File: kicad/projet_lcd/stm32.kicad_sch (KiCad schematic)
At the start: 36 parts, among them U1 STM32H563ZIT6, Y1 25MHZ, Y2 32.768KHZ

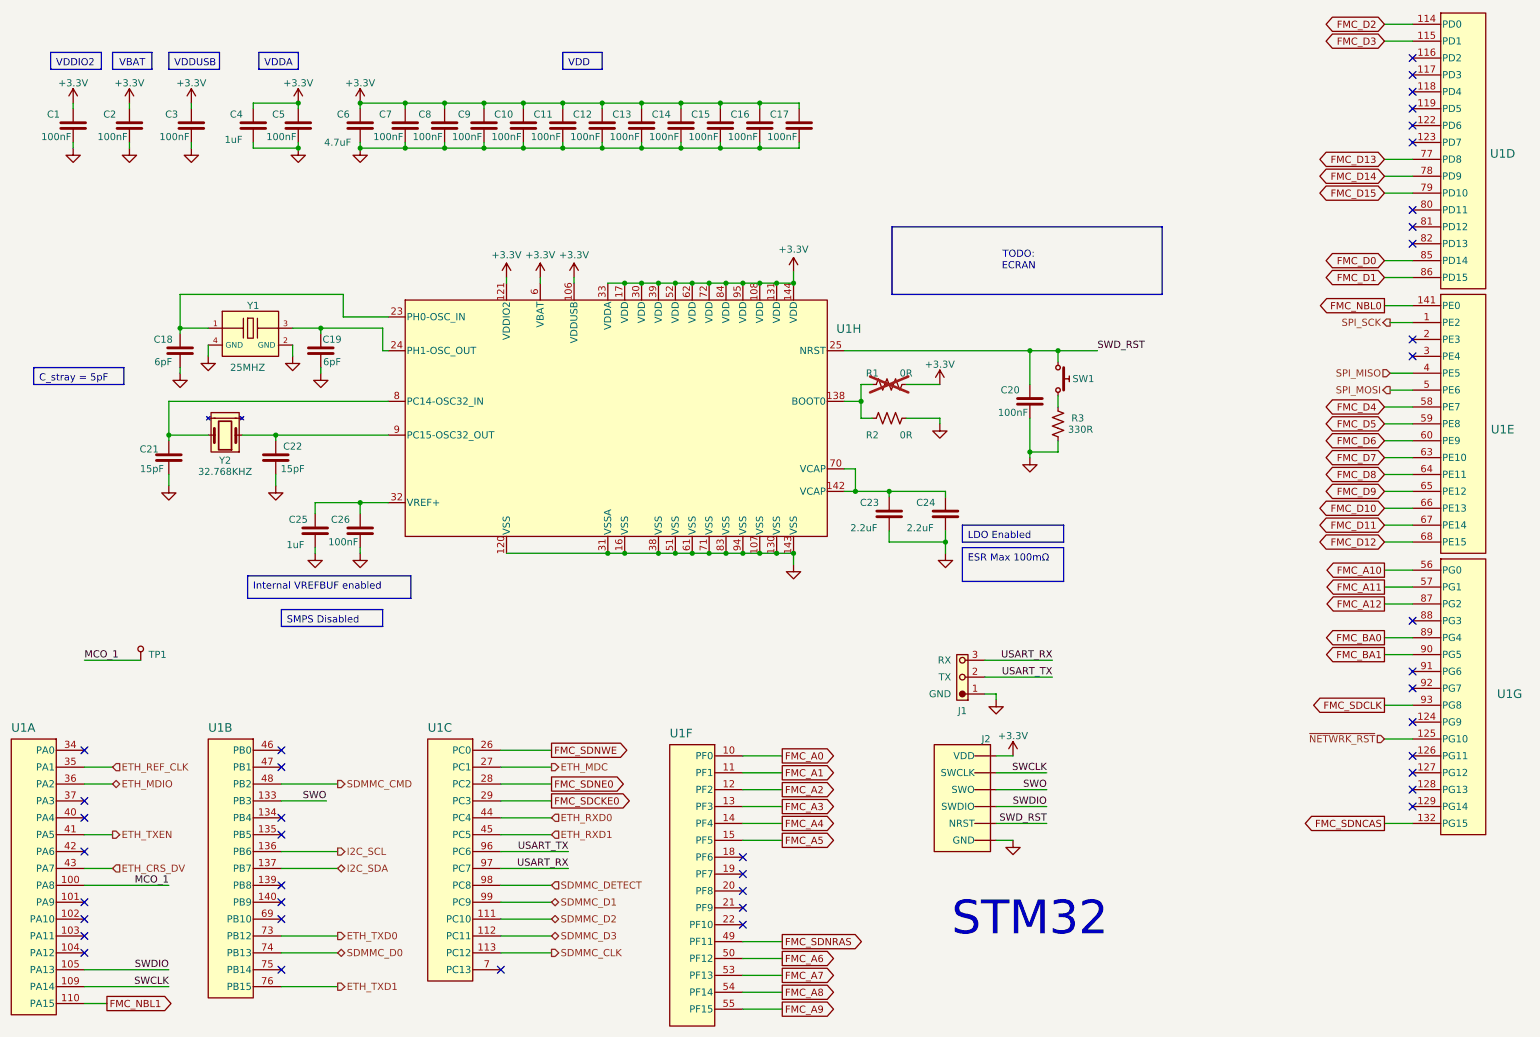
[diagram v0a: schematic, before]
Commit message: cleaning up ERC alerts
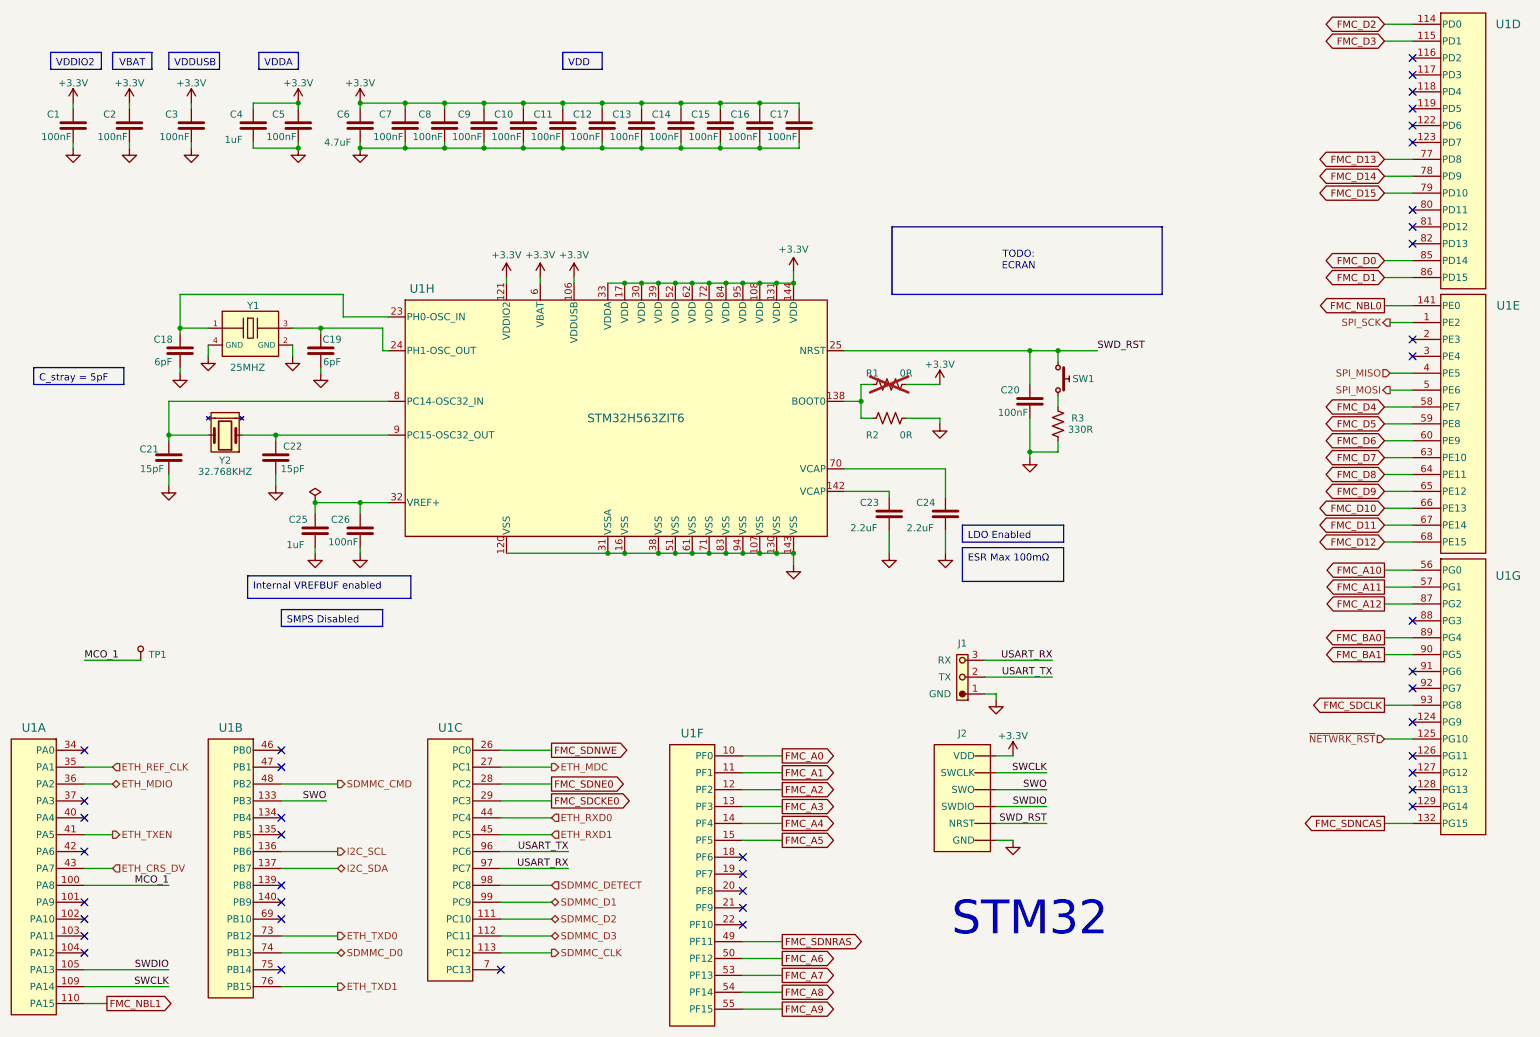
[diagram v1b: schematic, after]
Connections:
- net at C23.2, U1.142 (VCAP): no longer C24.2, U1.70 (VCAP)
- new net: C24.2, U1.70 (VCAP)
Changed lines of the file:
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@@
 	)
 	(junction
-		(at 77 30)
+		(at 69 101)
 		(diameter 0)
 		(color 0 0 0 0)
 	)
 	(junction
-		(at 85 30)
+		(at 77 30)
 		(diameter 0)
 		(color 0 0 0 0)
 	)
 	(junction
-		(at 124 110)
+		(at 85 30)
 		(diameter 0)
 		(color 0 0 0 0)
 	)
 	(junction
-		(at 196 74)
+		(at 124 110)
 		(diameter 0)
 		(color 0 0 0 0)
 	)
 	(junction
-		(at 165 99)
+		(at 196 74)
 		(diameter 0)
 		(color 0 0 0 0)
@@
 	)
 	(junction
-		(at 181 108)
-		(diameter 0)
-		(color 0 0 0 0)
-	)
-	(junction
 		(at 62 89)
 		(diameter 0)
@@
 	)
 	(junction
-		(at 171 99)
-		(diameter 0)
-		(color 0 0 0 0)
-	)
-	(junction
 		(at 92 30)
 		(diameter 0)
@@
 	(wire
 		(pts
-			(xy 171 99) (xy 181 99)
-		)
-		(stroke
-			(width 0)
-			(type default)
-		)
-	)
-	(wire
-		(pts
 			(xy 133 110) (xy 136 110)
 		)
@@
 	(wire
 		(pts
-			(xy 181 108) (xy 181 110)
-		)
-		(stroke
-			(width 0)
-			(type default)
-		)
-	)
-	(wire
-		(pts
 			(xy 134 38) (xy 134 37)
 		)
@@
 	(wire
 		(pts
-			(xy 165 99) (xy 171 99)
+			(xy 163 99) (xy 171 99)
 		)
 		(stroke
@@
 	(wire
 		(pts
-			(xy 165 95) (xy 163 95)
-		)
-		(stroke
-			(width 0)
-			(type default)
-		)
-	)
-	(wire
-		(pts
 			(xy 259 99) (xy 264 99)
 		)
@@
 	(wire
 		(pts
-			(xy 165 95) (xy 165 99)
-		)
-		(stroke
-			(width 0)
-			(type default)
-		)
-	)
-	(wire
-		(pts
 			(xy 259 116) (xy 264 116)
 		)
@@
 	(wire
 		(pts
-			(xy 181 99) (xy 181 100)
+			(xy 181 95) (xy 181 100)
 		)
 		(stroke
@@
 	(wire
 		(pts
-			(xy 163 99) (xy 165 99)
-		)
-		(stroke
-			(width 0)
-			(type default)
-		)
-	)
-	(wire
-		(pts
 			(xy 99 30) (xy 99 31)
 		)
@@
 	(wire
 		(pts
-			(xy 181 108) (xy 181 106)
+			(xy 181 106) (xy 181 110)
 		)
 		(stroke
@@
 	(wire
 		(pts
-			(xy 171 108) (xy 181 108)
-		)
-		(stroke
-			(width 0)
-			(type default)
-		)
-	)
-	(wire
-		(pts
 			(xy 120 38) (xy 127 38)
 		)
@@
 	(wire
 		(pts
-			(xy 171 106) (xy 171 108)
+			(xy 171 106) (xy 171 110)
 		)
 		(stroke
@@
 	(wire
 		(pts
+			(xy 163 95) (xy 181 95)
+		)
+		(stroke
+			(width 0)
+			(type default)
+		)
+	)
+	(wire
+		(pts
 			(xy 63 166) (xy 73 166)
 		)
@@
 	)
 	(symbol
+		(lib_name "STM32H563ZIT6_4")
 		(lib_id "MicroControllers:STM32H563ZIT6")
 		(at 82 65 0)
@@
 		(on_board yes)
 		(dnp no)
-		(fields_autoplaced yes)
 		(property "Reference" "U1"
-			(at 163.83 70.1198 0)
+			(at 88 63 0)
 			(effects
 				(font
@@
 		)
 		(property "Value" "STM32H563ZIT6"
-			(at 90 49 0)
+			(at 126 86 0)
 			(effects
 				(font
 					(size 1.524 1.524)
 				)
-				(hide yes)
 			)
 		)
@@
 	)
 	(symbol
+		(lib_name "STM32H563ZIT6_6")
 		(lib_id "MicroControllers:STM32H563ZIT6")
 		(at 28 145 0)
@@
 		(dnp no)
 		(property "Reference" "U1"
-			(at 15 141 0)
+			(at 19 141 0)
 			(effects
 				(font
 					(size 1.524 1.524)
 				)
-				(justify right)
 			)
 		)
@@
 		(dnp no)
 		(property "Reference" "U1"
-			(at 279 135 0)
+			(at 281 114 0)
 			(effects
 				(font
 					(size 1.524 1.524)
 				)
-				(justify left)
 			)
 		)
@@
 		(dnp no)
 		(property "Reference" "U1"
-			(at 280 39 0)
+			(at 281 16 0)
 			(effects
 				(font
@@
 		(dnp no)
 		(property "Reference" "U1"
-			(at 89 141 0)
+			(at 93 141 0)
 			(effects
 				(font
 					(size 1.524 1.524)
 				)
-				(justify right)
 			)
 		)
@@
 		(on_board yes)
 		(dnp no)
-		(fields_autoplaced yes)
 		(property "Reference" "J2"
-			(at 189 143 0)
+			(at 184 142 0)
 			(do_not_autoplace yes)
 			(effects
@@
 					(size 1.25 1.25)
 				)
-				(justify left)
 			)
 		)
@@
 		(dnp no)
 		(property "Reference" "J1"
-			(at 184 138 0)
+			(at 184 126 0)
 			(do_not_autoplace yes)
 			(effects
@@
 	)
 	(symbol
+		(lib_id "Power:GND")
+		(at 171 110 0)
+		(unit 1)
+		(exclude_from_sim no)
+		(in_bom yes)
+		(on_board yes)
+		(dnp no)
+		(fields_autoplaced yes)
+		(property "Reference" "#PWR097"
+			(at 171 116.35 0)
+			(effects
+				(font
+					(size 1.25 1.25)
+				)
+				(hide yes)
+			)
+		)
+		(property "Value" "GND"
+			(at 171 113.81 0)
+			(effects
+				(font
+					(size 1.25 1.25)
+				)
+				(hide yes)
+			)
+		)
+		(property "Footprint" ""
+			(at 171 110 0)
+			(effects
+				(font
+					(size 1.25 1.25)
+				)
+				(hide yes)
+			)
+		)
+		(property "Datasheet" ""
+			(at 171 110 0)
+			(effects
+				(font
+					(size 1.25 1.25)
+				)
+				(hide yes)
+			)
+		)
+		(property "Description" "Power symbol creates a global label with name \"GND\""
+			(at 173.54 120.668 0)
+			(effects
+				(font
+					(size 1.25 1.25)
+				)
+				(hide yes)
+			)
+		)
+		(pin "1"
+		)
+		(instances
+			(project "projet_lcd"
+				(path "/b3ce22de-813e-4a84-80c2-bec39c904000/9ea47d51-491e-4a8f-867a-699065ac1e83"
+					(reference "#PWR097")
+					(unit 1)
+				)
+			)
+		)
+	)
+	(symbol
 		(lib_id "Power:+3.3V")
 		(at 26 30 0)
@@
 		(dnp no)
 		(property "Reference" "U1"
-			(at 280 88 0)
+			(at 281 66 0)
 			(effects
 				(font
@@
 	)
 	(symbol
+		(lib_id "Power:PWR_FLAG")
+		(at 69 101 0)
+		(unit 1)
+		(exclude_from_sim no)
+		(in_bom yes)
+		(on_board yes)
+		(dnp no)
+		(fields_autoplaced yes)
+		(property "Reference" "#FLG07"
+			(at 69.5 114.5 0)
+			(effects
+				(font
+					(size 1.25 1.25)
+				)
+				(hide yes)
+			)
+		)
+		(property "Value" "PWR_FLAG"
+			(at 69 117 0)
+			(effects
+				(font
+					(size 1.25 1.25)
+				)
+				(hide yes)
+			)
+		)
+		(property "Footprint" ""
+			(at 69 101 0)
+			(effects
+				(font
+					(size 1.25 1.25)
+				)
+				(hide yes)
+			)
+		)
+		(property "Datasheet" ""
+			(at 69 101 0)
+			(effects
+				(font
+					(size 1.25 1.25)
+				)
+				(hide yes)
+			)
+		)
+		(property "Description" "Kicad strange way of managing power input/output pins"
+			(at 69 112 0)
+			(effects
+				(font
+					(size 1.25 1.25)
+				)
+				(hide yes)
+			)
+		)
+		(pin "1"
+		)
+		(instances
+			(project ""
+				(path "/b3ce22de-813e-4a84-80c2-bec39c904000/9ea47d51-491e-4a8f-867a-699065ac1e83"
+					(reference "#FLG07")
+					(unit 1)
+				)
+			)
+		)
+	)
+	(symbol
+		(lib_name "STM32H563ZIT6_5")
 		(lib_id "MicroControllers:STM32H563ZIT6")
 		(at 63 145 0)
@@
 		(dnp no)
 		(property "Reference" "U1"
-			(at 50 141 0)
+			(at 54 141 0)
 			(effects
 				(font
 					(size 1.524 1.524)
 				)
-				(justify right)
 			)
 		)
@@
 		(dnp no)
 		(property "Reference" "U1"
-			(at 132 142 0)
+			(at 136 142 0)
 			(effects
 				(font
 					(size 1.524 1.524)
 				)
-				(justify right)
 			)
 		)

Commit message: on avance !
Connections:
- net ETH_TXD1: now also U1.127 (PG12); no longer U1.76 (PB15)
- net SPI_MISO: now also U1.75 (PB14); no longer U1.4 (PE5)
- net SPI_MOSI: now also U1.76 (PB15); no longer U1.5 (PE6)
- net SPI_SCK: now also U1.69 (PB10); no longer U1.1 (PE2)
- net USART_RX: now also U1.102 (PA10); no longer U1.97 (PC7)
- net USART_TX: now also U1.101 (PA9); no longer U1.96 (PC6)
- net USB_DM: now reaches U1.103 (PA11)
- net USB_DP: now reaches U1.104 (PA12)
- net DISPLAY_MISO: now reaches U1.42 (PA6)
- net DISPLAY_CLK: now reaches U1.126 (PG11)
- net OUTPUT_9: now reaches U1.129 (PG14)
- net DISPLAY_PWM: now reaches U1.88 (PG3)
- net OUTPUT_7: now reaches U1.91 (PG6)
- net OUTPUT_2: now reaches U1.118 (PD4)
- net DISPLAY_MOSI: now reaches U1.123 (PD7)
- net DISPLAY_RST: now reaches U1.80 (PD11)
- net DISPLAY_RS: now reaches U1.81 (PD12)
- net DISPLAY_CS: now reaches U1.82 (PD13)
- net OUTPUT_3: now reaches U1.2 (PE3)
- net OUTPUT_4: now reaches U1.18 (PF6)
- net OUTPUT_5: now reaches U1.20 (PF8)
- net OUTPUT_6: now reaches U1.21 (PF9)
- net OUTPUT_8: now reaches U1.22 (PF10)
- new net OUTPUT_0: U1.96 (PC6)
- new net OUTPUT_1: U1.97 (PC7)
- no-connect marks 41 -> 22
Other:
- note removed: "TODO: ECRAN"

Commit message: routage en cours
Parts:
- J1: PIN_01 GND -> ## PIN1; PIN_02 TX -> ## PIN2; PIN_03 RX -> ## PIN3
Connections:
- net USB_DM: no longer names the net of U1.103 (PA11)
- net USB_DP: no longer names the net of U1.104 (PA12)
- no-connect marks 22 -> 24
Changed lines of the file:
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@@
 		)
 	)
+	(text_box "USB for later use ..."
+		(exclude_from_sim no)
+		(at 30 176 0)
+		(size 18 5)
+		(margins 0.9525 0.9525 0.9525 0.9525)
+		(stroke
+			(width 0)
+			(type solid)
+		)
+		(fill
+			(type none)
+		)
+		(effects
+			(font
+				(size 1.27 1.27)
+			)
+			(justify left top)
+		)
+	)
 	(text_box "VDDA"
 		(exclude_from_sim no)
@@
 	)
 	(no_connect
+		(at 28 178)
+	)
+	(no_connect
 		(at 28 157)
 	)
@@
 	)
 	(no_connect
+		(at 28 181)
+	)
+	(no_connect
 		(at 63 160)
 	)
@@
 	(wire
 		(pts
-			(xy 28 178) (xy 43 178)
-		)
-		(stroke
-			(width 0)
-			(type default)
-		)
-	)
-	(wire
-		(pts
-			(xy 28 181) (xy 43 181)
-		)
-		(stroke
-			(width 0)
-			(type default)
-		)
-	)
-	(wire
-		(pts
 			(xy 196 74) (xy 201 74)
 		)
@@
 		)
 	)
-	(label "USB_DM"
-		(at 43 178 180)
-		(effects
-			(font
-				(size 1.27 1.27)
-			)
-			(justify right bottom)
-		)
-	)
 	(label "SWDIO"
 		(at 43 184 180)
@@
 		)
 	)
-	(label "USB_DP"
-		(at 43 181 180)
-		(effects
-			(font
-				(size 1.27 1.27)
-			)
-			(justify right bottom)
-		)
-	)
 	(global_label "FMC_SDNRAS"
 		(shape output)
@@
 	)
 	(symbol
-		(lib_name "STM32H563ZIT6_4")
 		(lib_id "MicroControllers:STM32H563ZIT6")
 		(at 82 65 0)
@@
 	)
 	(symbol
-		(lib_name "STM32H563ZIT6_6")
 		(lib_id "MicroControllers:STM32H563ZIT6")
 		(at 28 145 0)
@@
 			)
 		)
-		(property "PIN_01" "GND"
+		(property "PIN_01" "## PIN1"
 			(at 182 135 0)
 			(do_not_autoplace yes)
@@
 			)
 		)
-		(property "PIN_02" "TX"
+		(property "PIN_02" "## PIN2"
 			(at 182 132 0)
 			(do_not_autoplace yes)
@@
 			)
 		)
-		(property "PIN_03" "RX"
+		(property "PIN_03" "## PIN3"
 			(at 182 129 0)
 			(do_not_autoplace yes)
@@
 	)
 	(symbol
-		(lib_name "STM32H563ZIT6_5")
 		(lib_id "MicroControllers:STM32H563ZIT6")
 		(at 63 145 0)

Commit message: schematiks seems okayish
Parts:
- removed SW1: ~, symbol Generics:SW_PushButton
- added SW1: ~, Misc:C284397, symbol Misc:sw_C2844397
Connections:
- net SWD_RST: now also SW1.1, SW1.2
- net at R3.2 (1): now also SW1.3, SW1.4
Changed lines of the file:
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@@
 	)
 	(symbol
+		(lib_id "Misc:sw_C2844397")
+		(at 201 76 270)
+		(unit 1)
+		(exclude_from_sim no)
+		(in_bom yes)
+		(on_board yes)
+		(dnp no)
+		(fields_autoplaced yes)
+		(property "Reference" "SW1"
+			(at 205.01 77.7299 90)
+			(effects
+				(font
+					(size 1.27 1.27)
+				)
+				(justify left)
+			)
+		)
+		(property "Value" "~"
+			(at 205.01 80.2699 90)
+			(effects
+				(font
+					(size 1.27 1.27)
+				)
+				(justify left)
+				(hide yes)
+			)
+		)
+		(property "Footprint" "Misc:C284397"
+			(at 208.5 79.5 0)
+			(effects
+				(font
+					(size 1.27 1.27)
+				)
+				(hide yes)
+			)
+		)
+		(property "Datasheet" ""
+			(at 201 76 0)
+			(effects
+				(font
+					(size 1.27 1.27)
+				)
+				(hide yes)
+			)
+		)
+		(property "Description" "Switch SPST"
+			(at 206 80 0)
+			(effects
+				(font
+					(size 1.27 1.27)
+				)
+				(hide yes)
+			)
+		)
+		(property "LCSC Part #" "C2844397"
+			(at 210.5 79.5 0)
+			(effects
+				(font
+					(size 1.27 1.27)
+				)
+				(hide yes)
+			)
+		)
+		(pin "3"
+		)
+		(pin "4"
+		)
+		(pin "2"
+		)
+		(pin "1"
+		)
+		(instances
+			(project ""
+				(path "/b3ce22de-813e-4a84-80c2-bec39c904000/9ea47d51-491e-4a8f-867a-699065ac1e83"
+					(reference "SW1")
+					(unit 1)
+				)
+			)
+		)
+	)
+	(symbol
 		(lib_id "Generics:C")
 		(at 47 37 90)
@@
 					(unit 1)
 				)
-			)
-		)
-	)
-	(symbol
-		(lib_id "Generics:SW_PushButton")
-		(at 201 76 270)
-		(unit 1)
-		(exclude_from_sim no)
-		(in_bom yes)
-		(on_board yes)
-		(dnp no)
-		(property "Reference" "SW1"
-			(at 205.5 79 90)
-			(do_not_autoplace yes)
-			(effects
-				(font
-					(size 1.25 1.25)
-				)
-			)
-		)
-		(property "Value" "~"
-			(at 190 80 0)
-			(effects
-				(font
-					(size 1.25 1.25)
-				)
-				(hide yes)
-			)
-		)
-		(property "Footprint" ""
-			(at 206.08 81 0)
-			(effects
-				(font
-					(size 1.25 1.25)
-				)
-				(hide yes)
-			)
-		)
-		(property "Datasheet" ""
-			(at 188 80 0)
-			(effects
-				(font
-					(size 1.25 1.25)
-				)
-				(hide yes)
-			)
-		)
-		(property "Description" "Push button switch, generic, two pins"
-			(at 197.1 79 0)
-			(effects
-				(font
-					(size 1.25 1.25)
-				)
-				(hide yes)
-			)
-		)
-		(property "Part#" ""
-			(at 201 76 0)
-			(effects
-				(font
-					(size 1.25 1.25)
-				)
-				(hide yes)
-			)
-		)
-		(property "Comments" ""
-			(at 201 76 0)
-			(effects
-				(font
-					(size 1.25 1.25)
-				)
-				(hide yes)
-			)
-		)
-		(pin "1"
-		)
-		(pin "2"
-		)
-		(instances
-			(project ""
-				(path "/b3ce22de-813e-4a84-80c2-bec39c904000/9ea47d51-491e-4a8f-867a-699065ac1e83"
-					(reference "SW1")
-					(unit 1)
-				)

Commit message: DRC / ERC ok
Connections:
- net LED_1: now reaches U1.1 (PE2)
- net LED_2: now reaches U1.3 (PE4)
- net LED_3: now reaches U1.4 (PE5)
- net LED_4: now reaches U1.140 (PB9)
- no-connect marks 24 -> 20
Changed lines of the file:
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@@
 		)
 	)
-	(text_box "Ajouter connecteur USB"
-		(exclude_from_sim no)
-		(at 113 122 0)
-		(size 27 5)
-		(margins 0.9525 0.9525 0.9525 0.9525)
-		(stroke
-			(width 0)
-			(type solid)
-		)
-		(fill
-			(type none)
-		)
-		(effects
-			(font
-				(size 1.27 1.27)
-				(color 255 3 64 1)
-			)
-			(justify left top)
-		)
-	)
 	(text_box "VDD\n"
 		(exclude_from_sim no)
@@
 	)
 	(no_connect
-		(at 63 172)
-	)
-	(no_connect
 		(at 264 140)
 	)
@@
 	)
 	(no_connect
-		(at 264 69)
-	)
-	(no_connect
 		(at 264 25)
 	)
@@
 	)
 	(no_connect
-		(at 264 75)
-	)
-	(no_connect
-		(at 264 78)
-	)
-	(no_connect
 		(at 28 181)
 	)
@@
 	(wire
 		(pts
+			(xy 259 75) (xy 264 75)
+		)
+		(stroke
+			(width 0)
+			(type default)
+		)
+	)
+	(wire
+		(pts
 			(xy 58 38) (xy 66 38)
 		)
@@
 	(wire
 		(pts
+			(xy 259 78) (xy 264 78)
+		)
+		(stroke
+			(width 0)
+			(type default)
+		)
+	)
+	(wire
+		(pts
 			(xy 109 61) (xy 109 62)
 		)
@@
 	(wire
 		(pts
+			(xy 63 172) (xy 73 172)
+		)
+		(stroke
+			(width 0)
+			(type default)
+		)
+	)
+	(wire
+		(pts
 			(xy 106 38) (xy 113 38)
 		)
@@
 	(wire
 		(pts
+			(xy 259 69) (xy 264 69)
+		)
+		(stroke
+			(width 0)
+			(type default)
+		)
+	)
+	(wire
+		(pts
 			(xy 199 152) (xy 190 152)
 		)
@@
 		)
 	)
+	(hierarchical_label "LED_1"
+		(shape output)
+		(at 259 69 180)
+		(effects
+			(font
+				(size 1.27 1.27)
+			)
+			(justify right)
+		)
+	)
+	(hierarchical_label "LED_3"
+		(shape output)
+		(at 259 78 180)
+		(effects
+			(font
+				(size 1.27 1.27)
+			)
+			(justify right)
+		)
+	)
 	(hierarchical_label "OUTPUT_6"
 		(shape bidirectional)
@@
 		)
 	)
+	(hierarchical_label "LED_4"
+		(shape output)
+		(at 73 172 0)
+		(effects
+			(font
+				(size 1.27 1.27)
+			)
+			(justify left)
+		)
+	)
 	(hierarchical_label "OUTPUT_2"
 		(shape bidirectional)
@@
 		)
 	)
+	(hierarchical_label "LED_2"
+		(shape output)
+		(at 259 75 180)
+		(effects
+			(font
+				(size 1.27 1.27)
+			)
+			(justify right)
+		)
+	)
